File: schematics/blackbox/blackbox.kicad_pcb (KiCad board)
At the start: 4 copper layers, 80 x 80 mm, 31 parts, among them J1 Micro_SD_Card, J104 SWD, J105 F_COMPUTER, J2 Micro_SD_Card, U101 MAX14787E, U102 STM32F405RGT6, Y101 26M

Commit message: Clean up board
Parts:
- moved J104 27.5 mm to (175.1, 157.3)
- moved C111 21.8 mm to (175.7, 164.2)
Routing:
- net /SWDIO: track 38.9 -> 20.4 mm
- net /SWDCLK: track 37.7 -> 20.5 mm
- net /NRST: track 43.8 -> 31.1 mm
- net /SPI3_MISO: track 57.2 -> 61.7 mm
- net /SPI2_MOSI: track 61.3 -> 64.4 mm
- net /SPI2_MISO: track 60.1 -> 63.2 mm
- net 3v3: track 12.6 -> 9.88 mm, vias 2 -> 11
- net /SPI3_MOSI: track 59.8 -> 61.1 mm
- net GND: track 51.3 -> 50.4 mm
- net /SPI3_SCLK: track 65.0 -> 65.5 mm

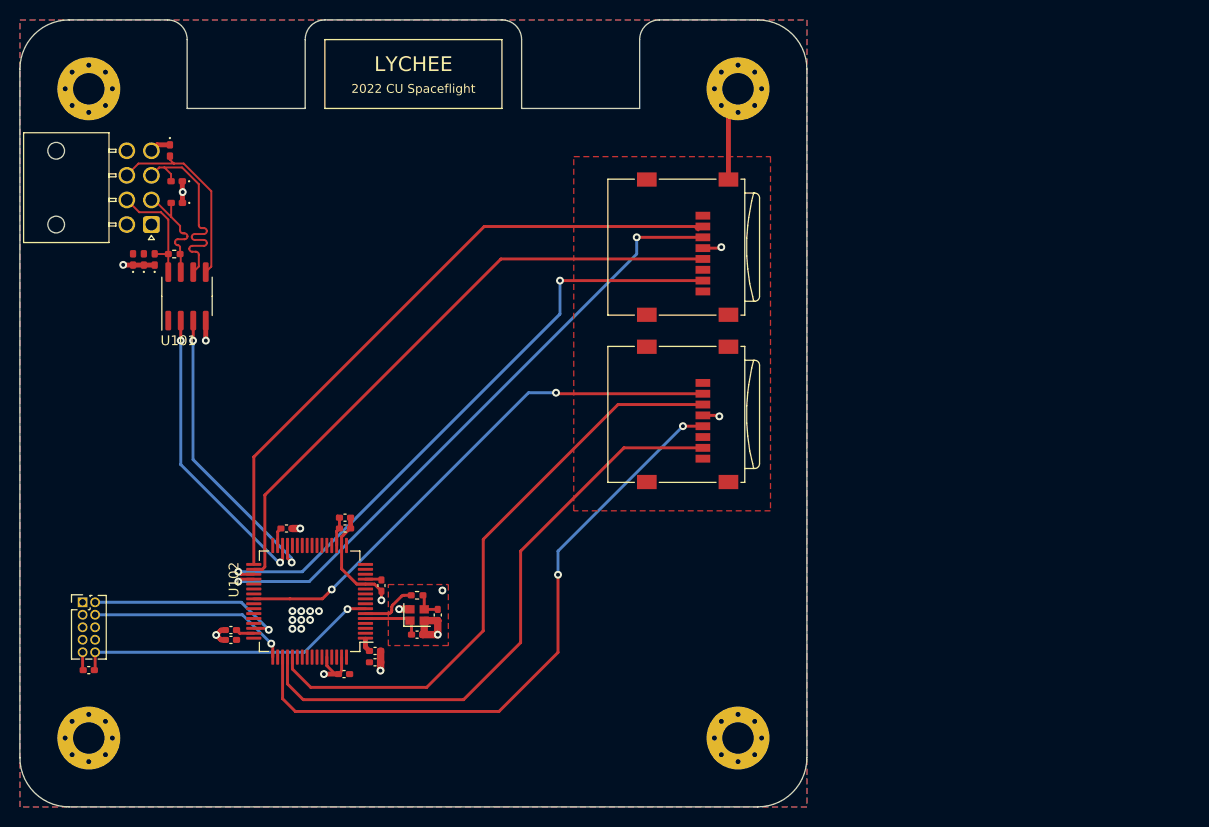
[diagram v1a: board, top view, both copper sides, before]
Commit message: Add power LED and test points
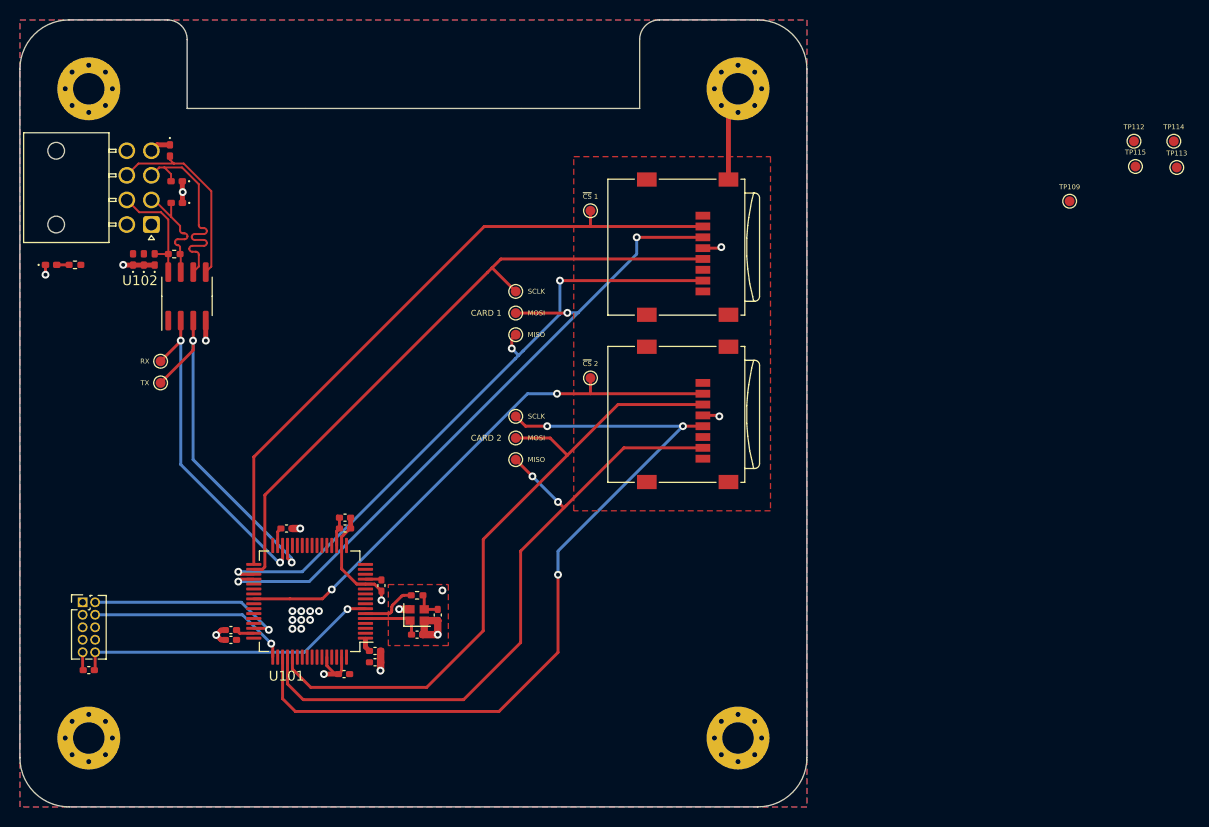
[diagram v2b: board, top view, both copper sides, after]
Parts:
- added D101: RED, Strix:LED_0402, F.Cu at (171.9, 123.0)
- added G***: LOGO, Strix:CUSF_Logo, B.Cu at (208.7, 122.0)
- added MISO: TestPoint, Strix:TestPoint, F.Cu at (219.1, 142.8)
- added MISO: TestPoint, Strix:TestPoint, F.Cu at (219.1, 130.1)
- added MOSI: TestPoint, Strix:TestPoint, F.Cu at (219.1, 127.9)
- added MOSI: TestPoint, Strix:TestPoint, F.Cu at (219.1, 140.6)
- added R101: 50, Strix:R_0402, F.Cu at (174.3, 123.0)
- added RX: TestPoint, Strix:TestPoint, F.Cu at (183.0, 132.8)
- added SCLK: TestPoint, Strix:TestPoint, F.Cu at (219.1, 125.7)
- added SCLK: TestPoint, Strix:TestPoint, F.Cu at (219.1, 138.4)
- added TP109: TestPoint, Strix:TestPoint, F.Cu at (275.4, 116.5)
- added TP112: TestPoint, Strix:TestPoint, F.Cu at (281.9, 110.4)
- added TP113: TestPoint, Strix:TestPoint, F.Cu at (286.3, 113.1)
- added TP114: TestPoint, Strix:TestPoint, F.Cu at (286.0, 110.4)
- added TP115: TestPoint, Strix:TestPoint, F.Cu at (282.1, 113.0)
- added TX: TestPoint, Strix:TestPoint, F.Cu at (183.0, 135.0)
- added ~{CS} 1: TestPoint, Strix:TestPoint, F.Cu at (226.7, 117.5)
- added ~{CS} 2: TestPoint, Strix:TestPoint, F.Cu at (226.7, 134.5)
- renumbered C105 to C102, C107 to C103, C112 to C104, C102 to C105, C108 to C107, C109 to C108, C110 to C109, C111 to C110, C103 to C111, C104 to C112, D104 to D102, D105 to D103, D106 to D104, D107 to D105, D108 to D106, D109 to D107, J1 to J101, J2 to J102, J104 to J103, J105 to J104, R101 to R103, U102 to U101, U101 to U102
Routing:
- net /SPI3_SCLK: track 65.5 -> 83.0 mm, vias 2 -> 3
- net /SPI3_MISO: track 61.7 -> 68.6 mm, vias 0 -> 2
- net /SPI2_MOSI: track 64.4 -> 70.8 mm, vias 2 -> 3
- net /SPI3_MOSI: track 61.1 -> 67.0 mm
- net /USART3_TX: track 30.6 -> 36.3 mm
- net /SPI2_SCLK: track 63.0 -> 66.4 mm
- net /USART3_RX: track 30.7 -> 33.6 mm
- net /SPI2_MISO: track 63.2 -> 65.7 mm, vias 2 -> 3
- net /SD2_~{CS}: track 54.4 -> 55.9 mm
- net Net-(D101-Pad2): track 0.00 -> 1.26 mm
- net /SD1_~{CS}: track 66.6 -> 67.9 mm
- net GND: track 50.4 -> 51.4 mm, vias 11 -> 12
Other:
- outline, holes or cut-outs redrawn
- board text added: "CARD 1"
- board text added: "CARD 2"
- board text added: "Jan. 2022"
- board text added: "Made in Cambridge, UK Designed by E. Clifford"
- board text removed: "2022 CU Spaceflight"
- board text removed: "LYCHEE"

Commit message: Final changes for manufacture (and silkscreen meme)
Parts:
- added G***: LOGO, Strix:Wimdy, F.Cu at (202.0, 125.2)
- moved GND 104.9 mm to (178.7, 128.7)
- moved 3.3V 95.0 mm to (181.2, 128.7)
- moved GND 77.0 mm to (216.1, 142.8)
- moved GND 72.2 mm to (216.1, 130.1)
- moved GND 57.9 mm to (226.7, 129.7)
- renumbered TP109 to 3.3V, TP112 to GND, TP113 to GND, TP115 to GND, TP114 to GND
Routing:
- net GND: track 51.4 -> 55.9 mm, vias 12 -> 15
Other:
- rule pad_to_mask_clearance: 0.05 -> 0
- board text added: "it fucken WIMDY"

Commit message: Fix library references
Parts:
- J101, J102: footprint Connector_Card:microSD_HC_Wuerth_693072010801 -> Strix:microSD_HC_Wuerth_693072010801
- TP101: renamed from ~{CS} 1
- TP102: renamed from ~{CS} 2
- renumbered RX to TP103, SCLK to TP104, SCLK to TP105, TX to TP106, MOSI to TP107, MOSI to TP108, 3.3V to TP109, MISO to TP110, MISO to TP111, GND to TP112, GND to TP113, GND to TP114, GND to TP115
